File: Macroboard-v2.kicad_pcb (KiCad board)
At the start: 2 copper layers, 7 parts, among them SW1 SW_Push, SW2 SW_Push, SW3 SW_Push, SW4 SW_Push, U1 XIAO-RP2040-DIP

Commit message: 20:49 - 2025-5-21
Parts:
- moved D2 40.6 mm to (156.5, 74.4)
- moved D1 40.1 mm to (188.0, 74.5)
- moved U1 39.1 mm to (171.5, 72.5)
- moved SW1 38.6 mm to (165.0, 89.4)
- moved SW2 38.6 mm to (184.4, 89.4)
- moved SW3 38.6 mm to (165.0, 108.5)
- moved SW4 38.6 mm to (184.4, 108.5)
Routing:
- net GND: track 0.00 -> 118.2 mm, vias 0 -> 1
- net +5V: track 0.00 -> 84.4 mm, vias 0 -> 2
- net Net-(U1-GPIO4/MISO): track 0.00 -> 61.6 mm, vias 0 -> 2
- net Net-(U1-GPIO3/MOSI): track 0.00 -> 60.0 mm, vias 0 -> 2
- net Net-(D1-VSS): track 0.00 -> 59.3 mm, vias 0 -> 3
- net Net-(U1-GPIO1/RX): track 0.00 -> 39.1 mm
- net Net-(D1-VDD): track 0.00 -> 25.2 mm, vias 0 -> 2
- net Net-(U1-GPIO2/SCK): track 0.00 -> 23.3 mm
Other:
- board outline added: 44.8 x 63.2 mm

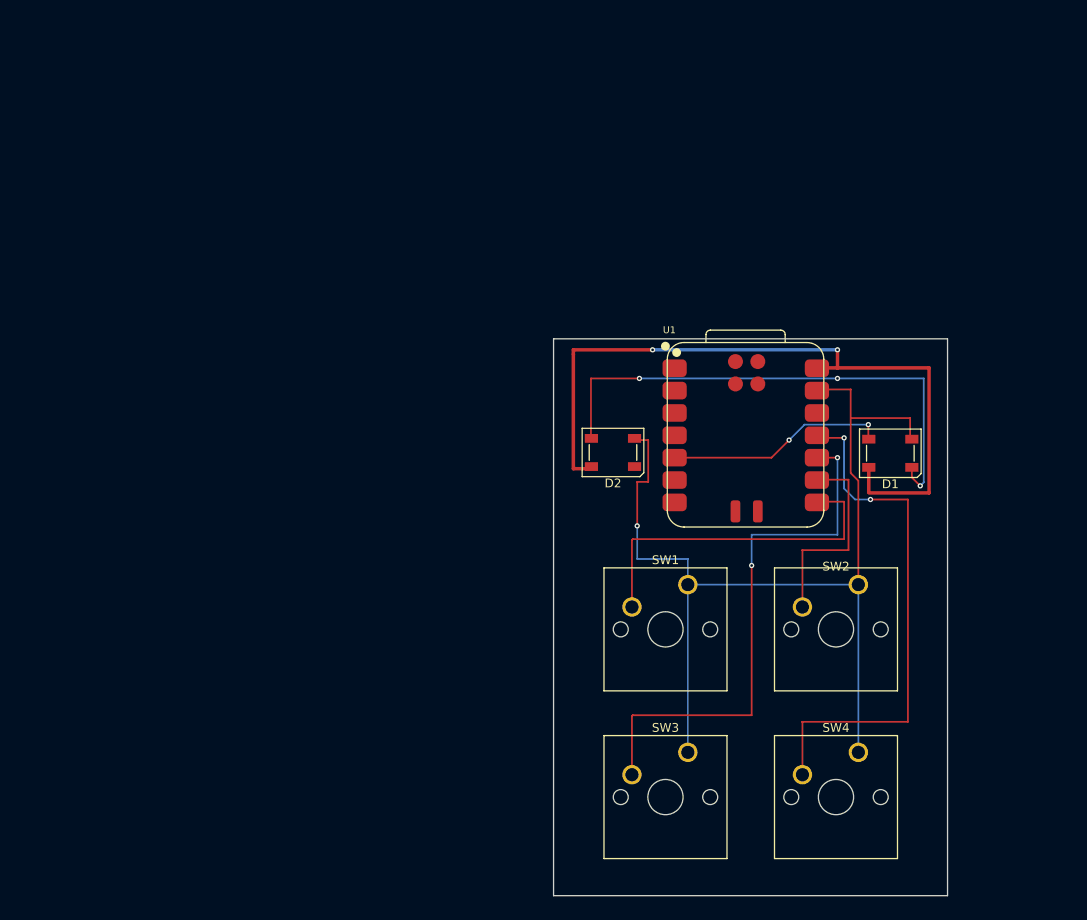
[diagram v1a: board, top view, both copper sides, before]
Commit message: Adding Rotary Encoder to the macroboard . Added led Light and added Hot swapable switches
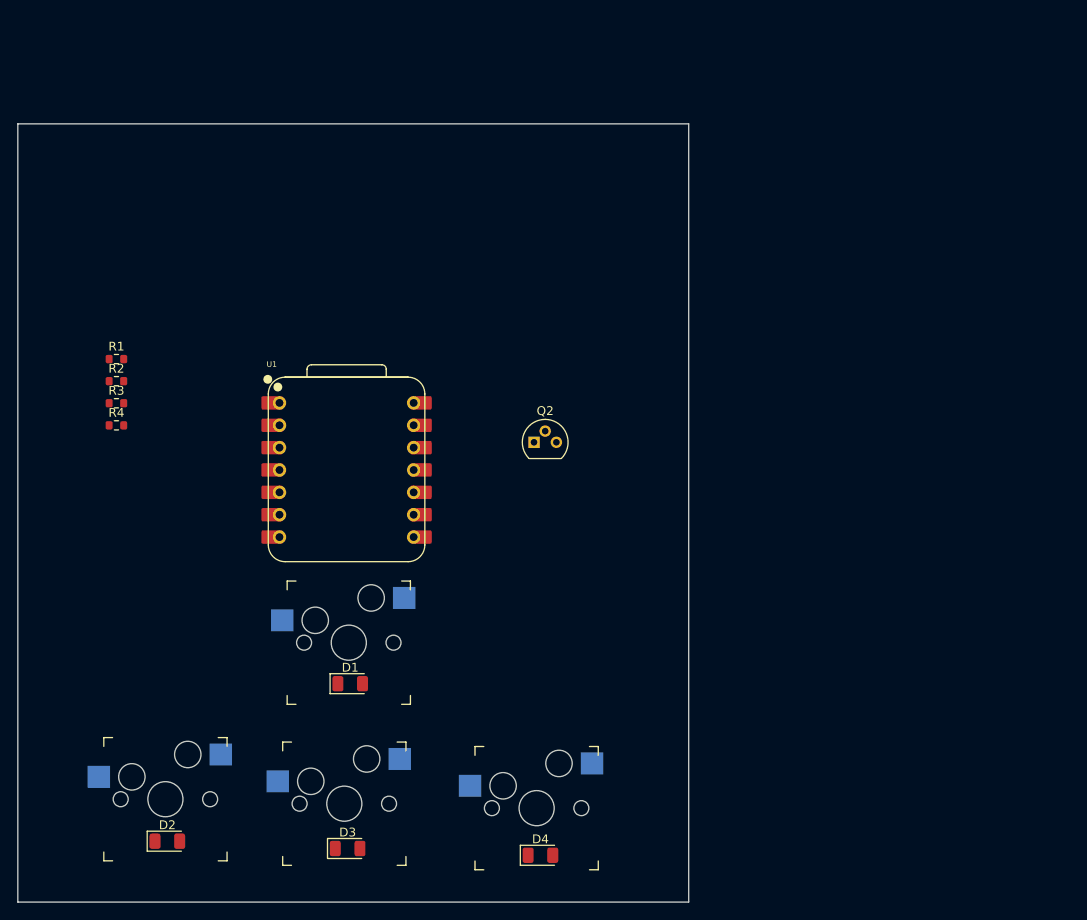
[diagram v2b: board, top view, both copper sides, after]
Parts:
- removed SW1, SW2, SW3, SW4: SW_Push, Button_Switch_Keyboard:SW_Cherry_MX_1.00u_PCB
- added D3: LED, LED_SMD:LED_1206_3216Metric, F.Cu at (126.4, 119.4)
- added D4: LED, LED_SMD:LED_1206_3216Metric, F.Cu at (148.3, 120.2)
- added Q2: Q_NPN_BEC, Package_TO_SOT_THT:TO-92, F.Cu at (147.5, 73.2)
- added R1: 68R, Resistor_SMD:R_0603_1608Metric, F.Cu at (100.1, 63.8)
- added R2: 68R, Resistor_SMD:R_0603_1608Metric, F.Cu at (100.1, 66.3)
- added R3: 68R, Resistor_SMD:R_0603_1608Metric, F.Cu at (100.1, 68.8)
- added R4: 68R, Resistor_SMD:R_0603_1608Metric, F.Cu at (100.1, 71.3)
- added SW5: SW_DIP_x01, MX Switch Hot Swapable:Kailh_socket_MX, F.Cu at (126.5, 96.0)
- added SW6: SW_DIP_x01, MX Switch Hot Swapable:Kailh_socket_MX, F.Cu at (105.7, 113.8)
- added SW7: SW_DIP_x01, MX Switch Hot Swapable:Kailh_socket_MX, F.Cu at (126.0, 114.3)
- added SW8: SW_DIP_x01, MX Switch Hot Swapable:Kailh_socket_MX, F.Cu at (147.8, 114.8)
- D1, D2: value SK6812 -> LED; footprint LED_SMD:LED_SK6812_PLCC4_5.0x5.0mm_P3.2mm -> LED_SMD:LED_1206_3216Metric
- U1: footprint OPKL:XIAO-RP2040-SMD -> OPKL:XIAO-RP2040-DIP
- moved D2 67.2 mm to (105.9, 118.6), turned to 0 degrees
- moved D1 66.7 mm to (126.7, 100.7), turned to 0 degrees
- moved U1 45.4 mm to (126.2, 76.4)
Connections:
- D1 pad 1: Net-(D1-VSS) -> GND
- D1 pad 2: GND -> Net-(D1-A)
- D2 pad 1: unconnected-(D2-VSS-Pad1) -> GND
- D2 pad 2: GND -> Net-(D2-A)
- U1 pad 1: unconnected-(U1-GPIO26/ADC0/A0-Pad1) -> Net-(Q2-B)
- U1 pad 11: Net-(U1-GPIO3/MOSI) -> unconnected-(U1-GPIO3/MOSI-Pad11)
- U1 pad 13: GND -> unconnected-(U1-GND-Pad13)
- U1 pad 14: +5V -> unconnected-(U1-VBUS-Pad14)
- U1 pad 2: unconnected-(U1-GPIO27/ADC1/A1-Pad2) -> Net-(U1-GPIO27/ADC1/A1)
- U1 pad 3: unconnected-(U1-GPIO28/ADC2/A2-Pad3) -> Net-(U1-GPIO28/ADC2/A2)
- U1 pad 4: unconnected-(U1-GPIO29/ADC3/A3-Pad4) -> Net-(U1-GPIO29/ADC3/A3)
- U1 pad 5: Net-(D1-VDD) -> unconnected-(U1-GPIO6/SDA-Pad5)
- U1 pad 7: unconnected-(U1-GPIO0/TX-Pad7) -> Net-(U1-GPIO0/TX)
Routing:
- net GND: track 118.2 -> 0.00 mm, vias 1 -> 0
- net +5V: track 84.4 -> 0.00 mm, vias 2 -> 0
- net Net-(U1-GPIO4/MISO): track 61.6 -> 0.00 mm, vias 2 -> 0
- net Net-(U1-GPIO3/MOSI): track 60.0 -> 0.00 mm, vias 2 -> 0
- net Net-(D1-VSS): track 59.3 -> 0.00 mm, vias 3 -> 0
- net Net-(S1-COMMON): track 39.1 -> 0.00 mm
- net Net-(D1-VDD): track 25.2 -> 0.00 mm, vias 2 -> 0
- net Net-(S1-CHANNEL_A): track 23.3 -> 0.00 mm
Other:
- board size 44.8 x 63.2 mm -> 76.2 x 88.4 mm

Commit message: Schemetics and PCB Desing completed . T- 1756 -20250522
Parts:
- added S2: PEC12R-4015F-S0024, PEC12R-4015F-S0024 Rotary Encoder:XDCR_PEC12R-4015F-S0024, F.Cu at (147.6, 93.2)
- Q2: footprint Package_TO_SOT_THT:TO-92 -> Transistor:SOT-23
- moved R3 63.4 mm to (137.5, 120.0)
- moved R4 58.9 mm to (148.4, 105.0)
- moved R2 56.0 mm to (116.2, 120.0)
- moved R1 51.5 mm to (137.2, 99.6)
- moved Q2 42.0 mm to (118.6, 103.7)
- moved U1 25.6 mm to (106.6, 92.9)
- moved D1 3.12 mm to (127.8, 97.8)
- moved SW5 3.03 mm to (126.8, 93.0)
- moved D4 1.16 mm to (148.2, 119.0)
- moved SW7 0.94 mm to (126.9, 114.2)
- moved D3 0.75 mm to (127.0, 119.0)
- moved SW8 0.66 mm to (148.1, 114.2)
- moved SW6 0.41 mm to (105.7, 114.2)
- moved D2 0.37 mm to (105.9, 118.9)
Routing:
- net GND: track 0.00 -> 126.3 mm, vias 0 -> 7
- net Net-(U1-GPIO27/ADC1/A1): track 0.00 -> 83.8 mm
- net Net-(Q2-E): track 0.00 -> 71.6 mm
- net Net-(U1-GPIO0/TX): track 0.00 -> 59.8 mm, vias 0 -> 2
- net Net-(U1-GPIO28/ADC2/A2): track 0.00 -> 48.4 mm
- net Net-(S2-CHANNEL_A): track 0.00 -> 43.5 mm, vias 0 -> 3
- net Net-(S2-COMMON): track 0.00 -> 41.5 mm, vias 0 -> 1
- net Net-(U1-GPIO4/MISO): track 0.00 -> 39.5 mm
- net Net-(Q2-B): track 0.00 -> 35.5 mm
- net Net-(D4-A): track 0.00 -> 33.0 mm
- net Net-(U1-GPIO29/ADC3/A3): track 0.00 -> 26.2 mm
- net Net-(D2-A): track 0.00 -> 9.53 mm
- net Net-(D3-A): track 0.00 -> 9.35 mm
- net Net-(D1-A): track 0.00 -> 9.02 mm
- added copper zone on F.Cu, net GND
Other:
- board size 76.2 x 88.4 mm -> 62.2 x 42.5 mm
